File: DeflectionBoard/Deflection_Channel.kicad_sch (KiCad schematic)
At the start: 31 parts, among them J201 YOKE_X, U201 CSD97394Q4M, U202 CSD97394Q4M, U203 INA240A1D, U204 OPA2196xD, U205 TLV3501AID, U206 74LVC1G04, U207 74LVC1G08, U208 74LVC1G08

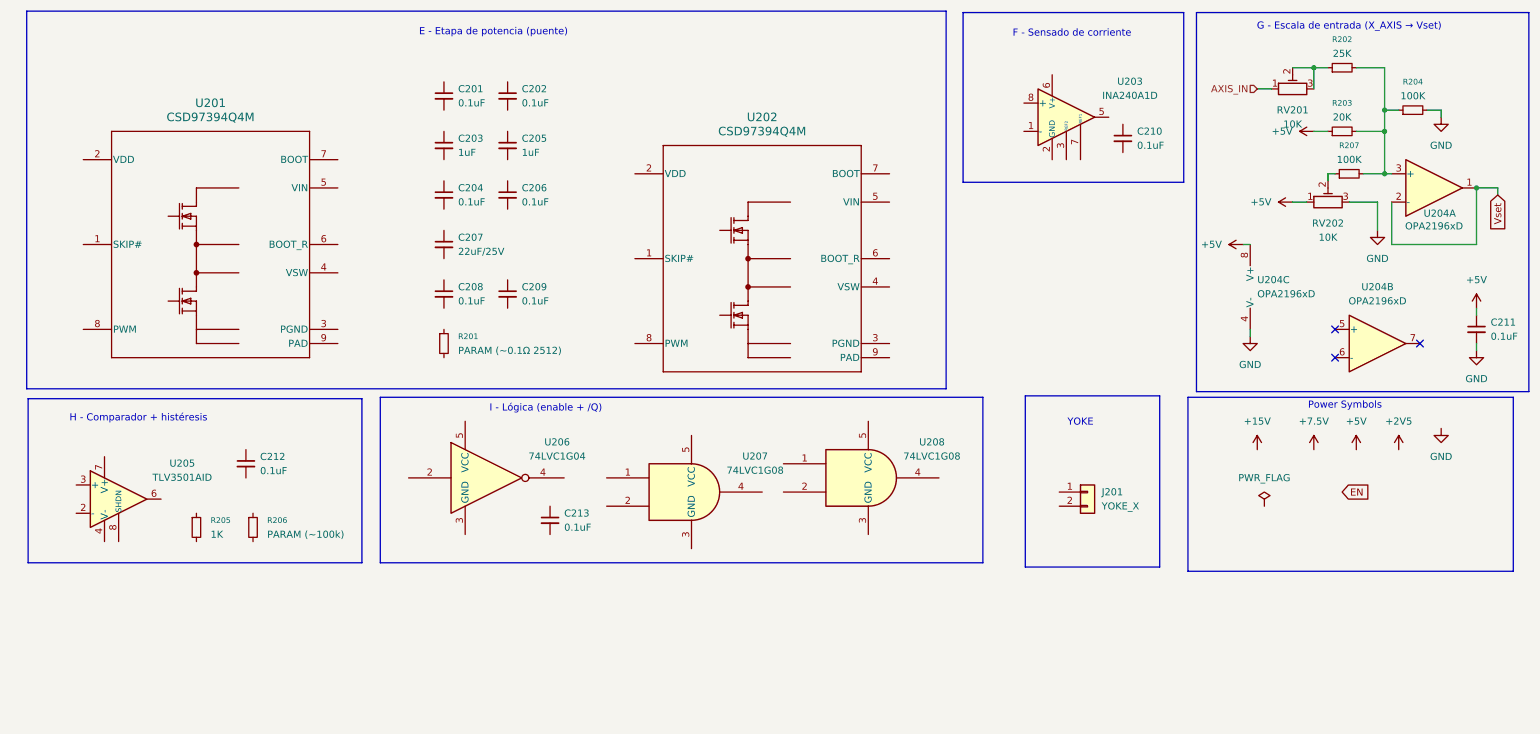
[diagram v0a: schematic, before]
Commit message: DeflectionBoard: channel X + power schematic complete, ERC clean
Full-bridge hysteretic current-mode deflection channel (CSD97394Q4M),
INA240 current sense, OPA2196 input scale, TLV3501 comparator, EN pull-up.
Power: TPS55340 boost (R106=78.7k/~600kHz), AP63205 buck 5V, REF3325 Vmid.
Hierarchical: root + Power + Deflection_Channel sheets, AXIS_IN sheet pin
wired to input connector. 0 ERC violations.

Co-Authored-By: Claude Opus 4.8 <noreply@anthropic.com>
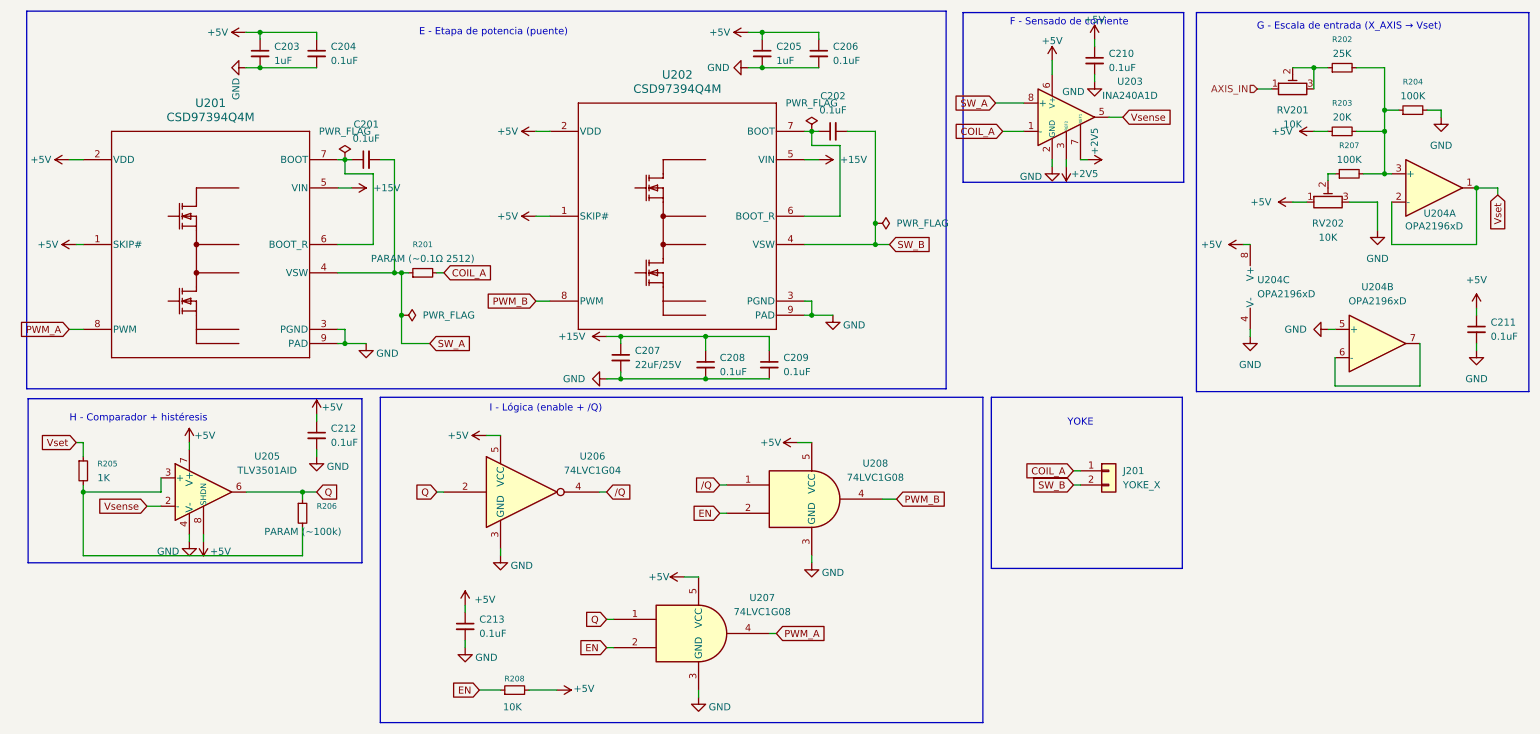
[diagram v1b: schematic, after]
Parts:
- added R208: 10K, symbol Device:R_Small
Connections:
- net +15V: now also C207.1, C208.1, C209.1, U201.5 (VIN), U202.5 (VIN)
- net +2V5: now also U203.3 (REF2), U203.7 (REF1)
- net +5V: now also C203.1, C204.1, C205.1, C206.1, C210.1, C212.1, C213.1, U201.1 (SKIP#), U201.2 (VDD), U202.1 (SKIP#), U202.2 (VDD), U203.6 (V+), U205.7 (V+), U205.8 (SHDN), U206.5 (VCC), U207.5 (VCC), U208.5 (VCC), R208.2
- net EN: now also U207.2, U208.2, R208.1
- net GND: now also C203.2, C204.2, C205.2, C206.2, C207.2, C208.2, C209.2, C210.2, C212.2, C213.2, U201.3 (PGND), U201.9 (PAD), U202.3 (PGND), U202.9 (PAD), U203.2 (GND), U203.4 (GND), U204.5 (+), U205.4 (V-), U206.3 (GND), U207.3 (GND), U208.3 (GND)
- net Vset: now also R205.1
- net Q: now reaches U207.1
- net Q: now also R206.1, U205.6, U206.2
- net PWM_A: now reaches U207.4
- net PWM_A: now also U201.8 (PWM)
- net at C202.1: now also U202.6 (BOOT_R), U202.7 (BOOT)
- net SW_B: now reaches C202.2
- net SW_B: now also J201.2 (Pin_2), U202.4 (VSW)
- net at R206.2: now also R205.2, U205.3 (+)
- net at C201.1: now also U201.6 (BOOT_R), U201.7 (BOOT)
- net SW_A: now reaches C201.2
- net SW_A: now also R201.1, U201.4 (VSW), U203.8 (+)
- net /Q: now reaches U206.4
- net /Q: now also U208.1
- net Vsense: now reaches U205.2 (-)
- net Vsense: now also U203.5
- net PWM_B: now reaches U208.4
- net PWM_B: now also U202.8 (PWM)
- net at U204.6 (-): now also U204.7
- net COIL_A: now reaches U203.1 (-)
- net COIL_A: now also J201.1 (Pin_1), R201.2
- no-connect marks 3 -> 0
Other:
- note removed: "Power Symbols"
- moved on the sheet: C201, C202, C203, C204, C205, C206, C207, C208, C209, C210, C212, C213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

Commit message: DeflectionBoard: channel Y instanced, footprints assigned, ERC clean
- Y axis = 2nd instance of Deflection_Channel sheet (X=2xx, Y=3xx)
- Signal labels made local (per-instance scoping), power refs uniquified
- Footprints: 0402 passives, R201/R301 shunt=2512, D102=SS54/SMB,
  J1=PH 4p / J101=VH power / yoke=XH (keyed), L101=12x12 / L102=SRN6045
- E96 1% feedback/timing resistors (137k/53.6k/78.7k)

Co-Authored-By: Claude Opus 4.8 <noreply@anthropic.com>
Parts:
- C201, C202, C203, C204, C205, C206, C208, C209, C210, C211, C212, C213: footprint (none) -> Capacitor_SMD:C_0402_1005Metric
- C207: footprint (none) -> Capacitor_SMD:C_1206_3216Metric
- J201: value YOKE_X -> YOKE; footprint (none) -> Connector_JST:JST_XH_B2B-XH-AM_1x02_P2.50mm_Vertical
- R201: footprint (none) -> Resistor_SMD:R_2512_6332Metric
- R202, R203, R204, R205, R206, R207, R208: footprint (none) -> Resistor_SMD:R_0402_1005Metric
- RV201, RV202: footprint (none) -> Potentiometer_THT:Potentiometer_Bourns_3339H_Vertical
- U206, U207, U208: footprint (none) -> Package_TO_SOT_SMD:SOT-23-5
